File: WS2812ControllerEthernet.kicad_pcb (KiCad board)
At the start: 2 copper layers, 26.9 x 59.8 mm, 11 parts, among them J1 Conn_01x04_Male, J2 Conn_01x03_Male, J3 Conn_01x04_Male, J4 Conn_01x02_Male, U1 WT32_ETH01

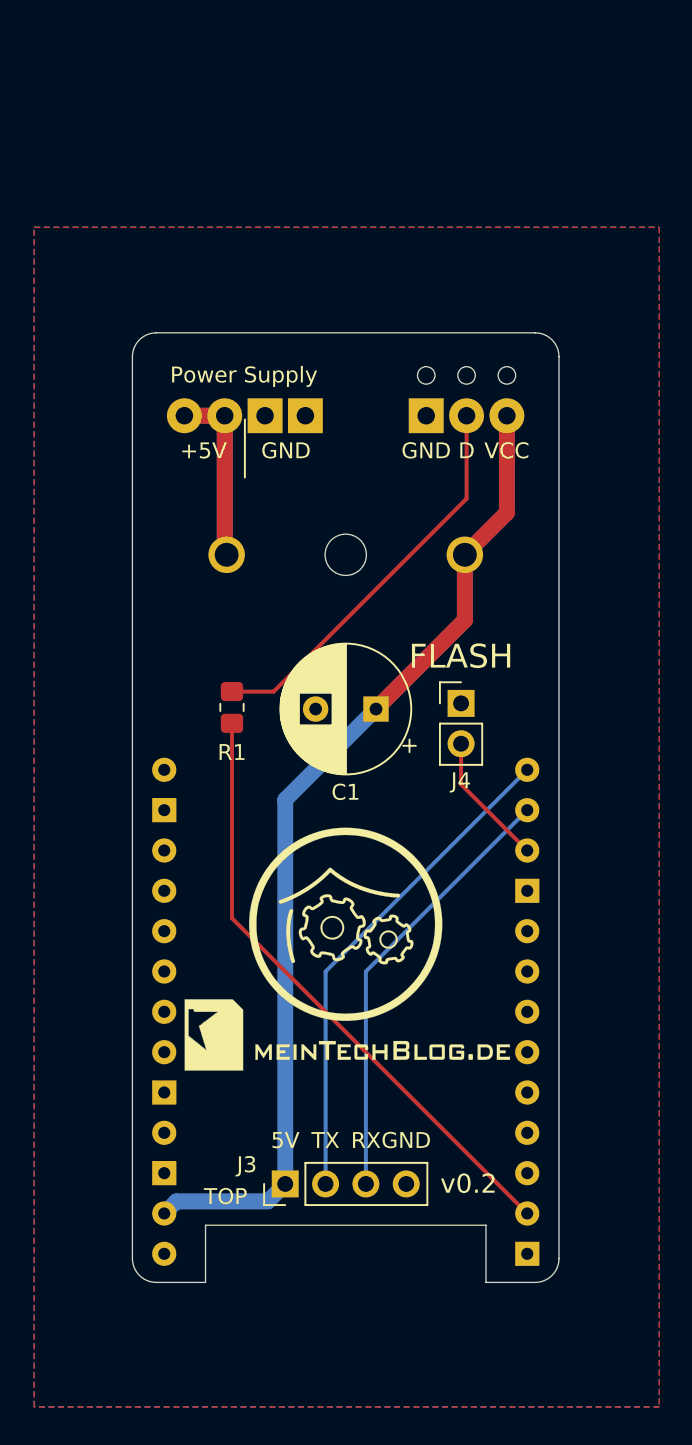
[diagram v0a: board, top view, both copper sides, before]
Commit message: Added level shifter
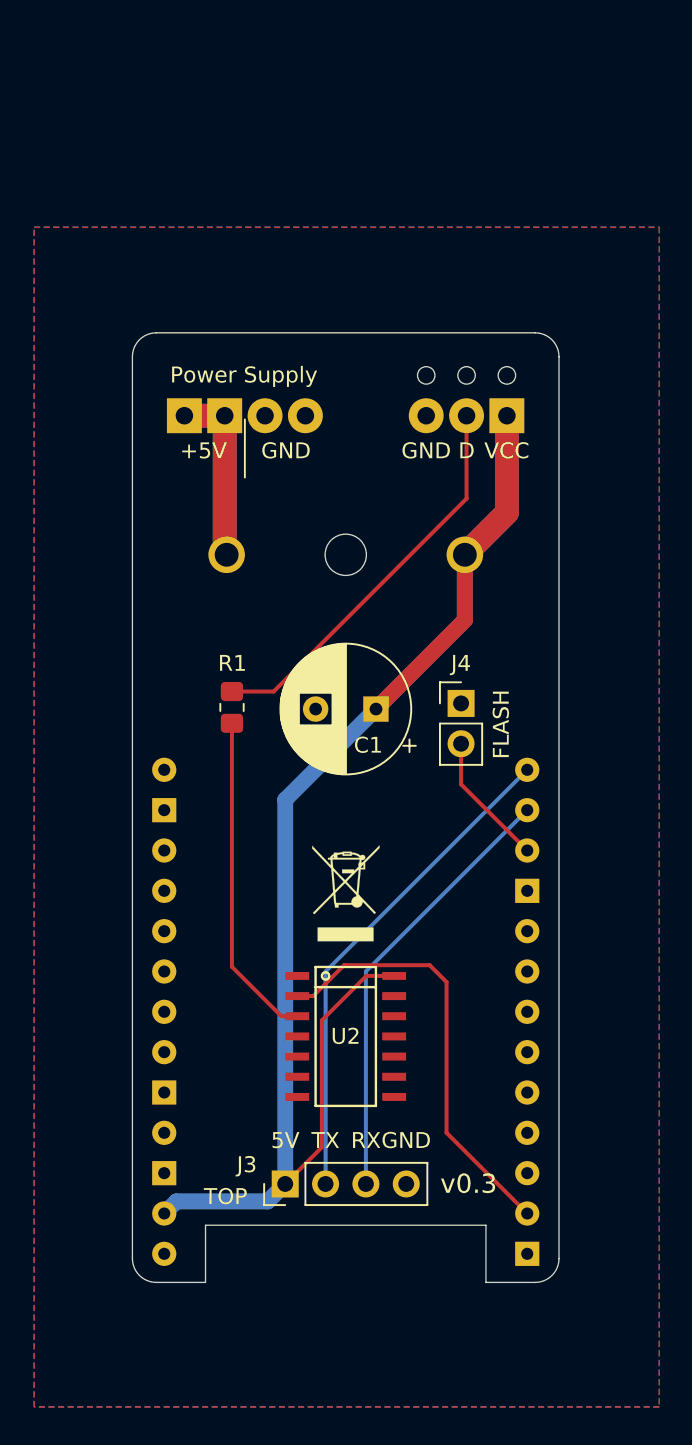
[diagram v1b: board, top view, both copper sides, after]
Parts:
- added U2: SN74AHCT125, halibs:SN74AHCT125D, F.Cu at (146.6, 90.5)
- G*** (x2): moved to B.Cu
- REF**: moved to F.Cu
- moved REF** 18.4 mm to (146.6, 87.3), turned to 0 degrees
- moved G*** 8.41 mm to (139.1, 92.5), turned to 90 degrees
- moved G*** 5.88 mm to (148.4, 94.8), turned to 90 degrees
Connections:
- net /DATA renamed Net-(J2-Pad2)
- R1 pad 2: GPIO2 -> DATA
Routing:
- net DATA: track 0.00 -> 20.7 mm
- net +5V: track 84.6 -> 101.6 mm
- net GPIO2: track 38.6 -> 27.3 mm
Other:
- net class Fet: trace_width 1 -> 1.5
- board text added: "5A max."
- board text added: "v0.3"
- board text removed: "Max. 6A !"
- board text removed: "v0.2"

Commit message: Updated to KiCad 6
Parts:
- U1: footprint halibs:WT32_ETH01 -> haus-automatisierung:WT32_ETH01
- U2: footprint halibs:SN74AHCT125D -> haus-automatisierung:SN74AHCT125D
- moved G*** 1.93 mm to (146.6, 94.2)
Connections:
- U1 pad 1: Net-(U1-Pad1) -> unconnected-(U1-Pad1)
- U1 pad 10: Net-(U1-Pad10) -> unconnected-(U1-Pad10)
- U1 pad 13: Net-(U1-Pad13) -> unconnected-(U1-Pad13)
- U1 pad 17: Net-(U1-Pad17) -> unconnected-(U1-Pad17)
- U1 pad 18: Net-(U1-Pad18) -> unconnected-(U1-Pad18)
- U1 pad 19: Net-(U1-Pad19) -> unconnected-(U1-Pad19)
- U1 pad 2: Net-(U1-Pad2) -> unconnected-(U1-Pad2)
- U1 pad 20: Net-(U1-Pad20) -> unconnected-(U1-Pad20)
- U1 pad 21: Net-(U1-Pad21) -> unconnected-(U1-Pad21)
- U1 pad 22: Net-(U1-Pad22) -> unconnected-(U1-Pad22)
- U1 pad 23: Net-(U1-Pad23) -> unconnected-(U1-Pad23)
- U1 pad 24: Net-(U1-Pad24) -> unconnected-(U1-Pad24)
- U1 pad 26: Net-(U1-Pad26) -> unconnected-(U1-Pad26)
- U1 pad 3: Net-(U1-Pad3) -> unconnected-(U1-Pad3)
- U1 pad 4: Net-(U1-Pad4) -> unconnected-(U1-Pad4)
- U1 pad 5: Net-(U1-Pad5) -> unconnected-(U1-Pad5)
- U1 pad 6: Net-(U1-Pad6) -> unconnected-(U1-Pad6)
- U1 pad 7: Net-(U1-Pad7) -> unconnected-(U1-Pad7)
- U1 pad 8: Net-(U1-Pad8) -> unconnected-(U1-Pad8)
- U1 pad 9: Net-(U1-Pad9) -> unconnected-(U1-Pad9)
- U2 pad 11: Net-(U2-Pad11) -> unconnected-(U2-Pad11)
- U2 pad 12: Net-(U2-Pad12) -> unconnected-(U2-Pad12)
- U2 pad 5: Net-(U2-Pad5) -> unconnected-(U2-Pad5)
- U2 pad 6: Net-(U2-Pad6) -> unconnected-(U2-Pad6)
- U2 pad 8: Net-(U2-Pad8) -> unconnected-(U2-Pad8)
- U2 pad 9: Net-(U2-Pad9) -> unconnected-(U2-Pad9)
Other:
- net class Default removed
- net class Fet removed

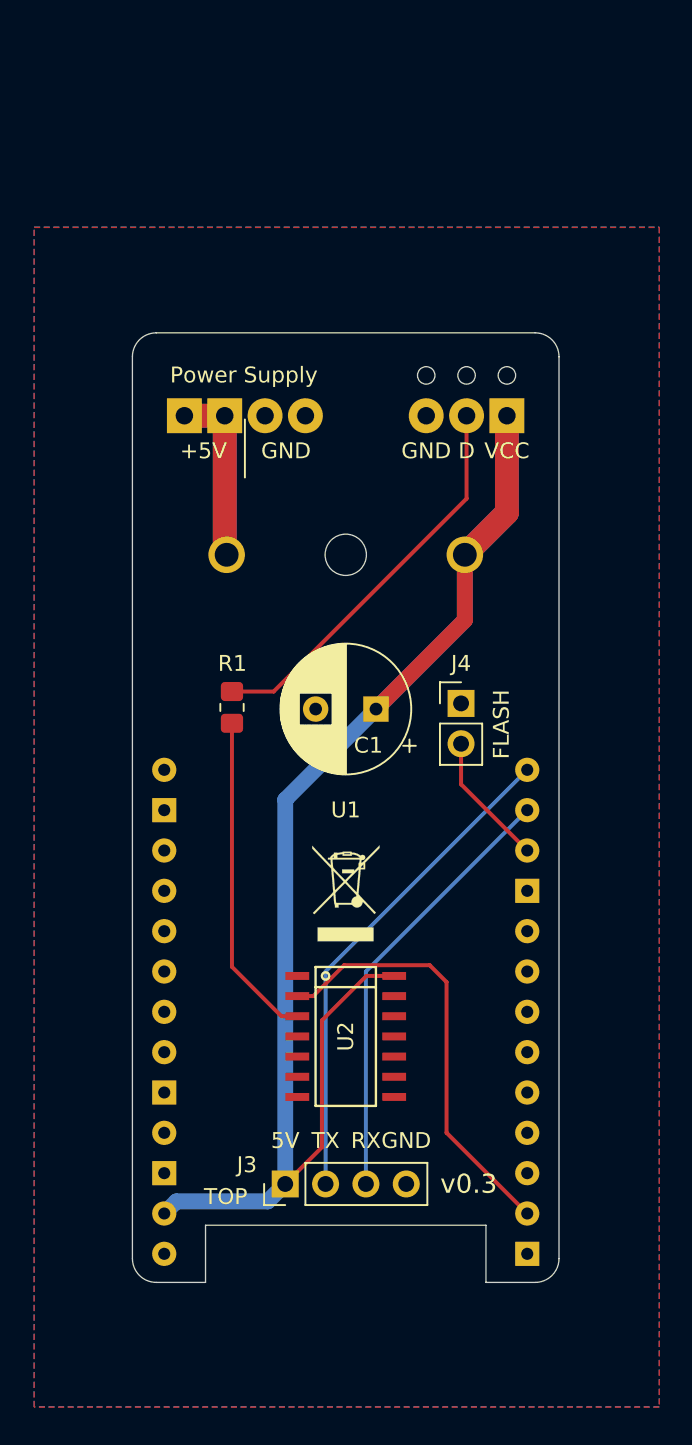
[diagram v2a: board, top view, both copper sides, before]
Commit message: Updated layout
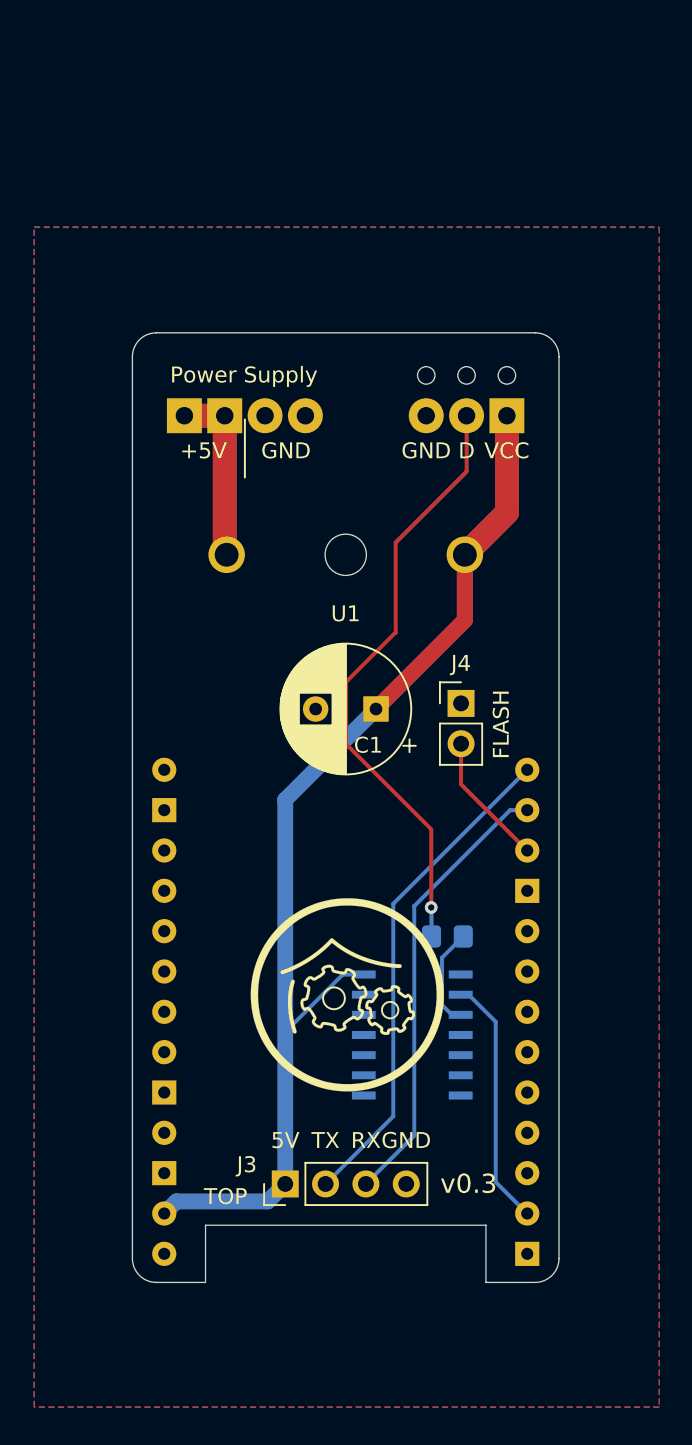
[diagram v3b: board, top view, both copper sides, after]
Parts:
- removed the G*** at (139.1, 92.5)
- added G***: LOGO, haus-automatisierung:QRCode-hausauto_10mm, B.Cu at (144.0, 85.8)
- added G***: LOGO, haus-automatisierung:meintechblog, B.Cu at (139.2, 91.8)
- G***: moved to F.Cu
- R1, REF**, U2: moved to B.Cu
- moved R1 19.8 mm to (153.0, 90.0), turned to 0 degrees
- moved REF** 14.2 mm to (139.0, 75.2), turned to 180 degrees
- moved U2 4.19 mm to (150.7, 90.4), turned to 180 degrees
- moved G*** 0.55 mm to (146.7, 93.7), turned to 0 degrees
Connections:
- U1 pad 17: unconnected-(U1-Pad17) -> GND
- U1 pad 2: unconnected-(U1-Pad2) -> GND
- U1 pad 26: unconnected-(U1-Pad26) -> GND
- U1 pad 9: unconnected-(U1-Pad9) -> GND
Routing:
- net DATA: track 20.7 -> 6.30 mm
- net Net-(J2-Pin_2): track 25.0 -> 38.2 mm, vias 0 -> 1
- net GPIO2: track 27.3 -> 15.8 mm
- net +5V: track 101.4 -> 90.9 mm
- net /RX: track 27.7 -> 28.4 mm

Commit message: Added additional GPIO for strip
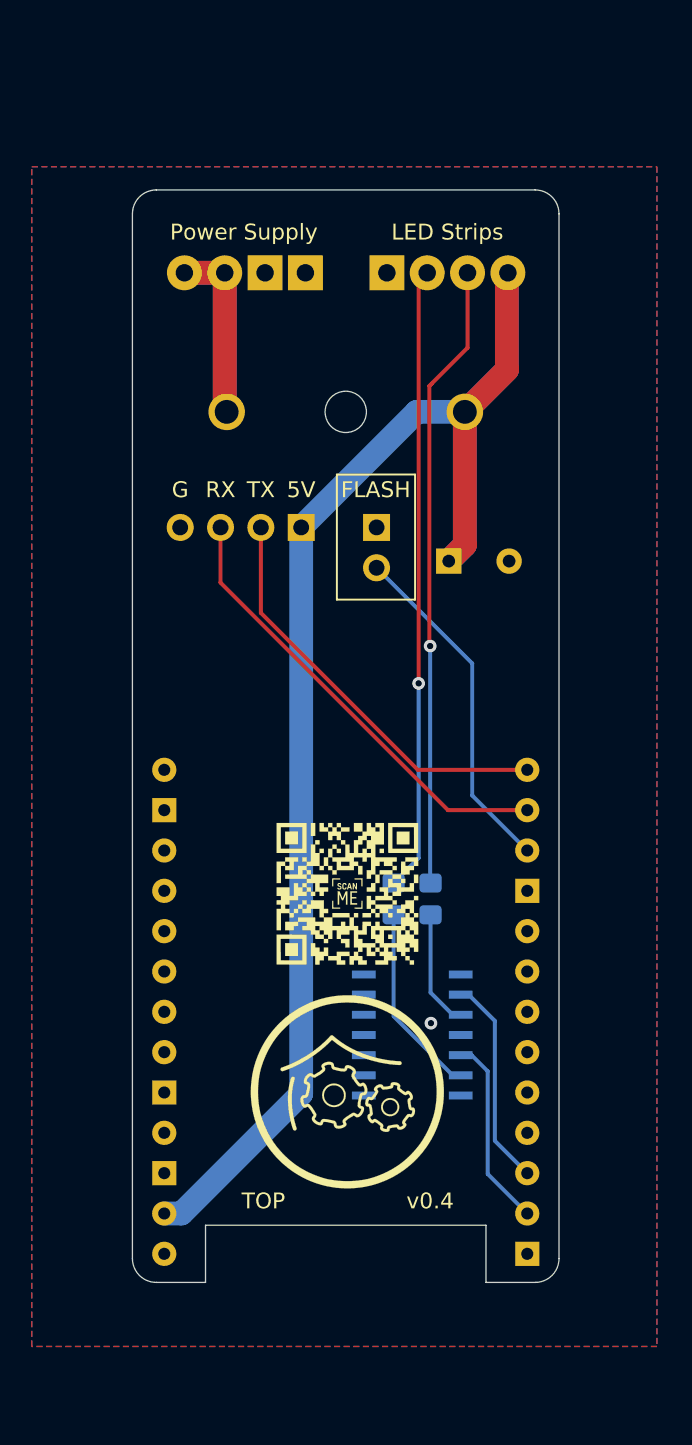
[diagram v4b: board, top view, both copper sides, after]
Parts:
- removed the G*** at (146.7, 93.7)
- removed the G*** at (139.2, 91.8)
- removed REF**: WEEE-Logo_4.2x6mm_SilkScreen, Symbol:WEEE-Logo_4.2x6mm_SilkScreen
- added G***: LOGO, haus-automatisierung:Logo, F.Cu at (146.7, 99.8)
- added R2: R, Resistor_SMD:R_0805_2012Metric_Pad1.20x1.40mm_HandSolder, B.Cu at (149.6, 87.7)
- C1, J3, J4: moved to B.Cu
- F1: footprint halibs:Fuse-PTF75_Stelvio -> haus-automatisierung:Fuse-PTF75_Stelvio
- G2: renamed from G***; moved to F.Cu
- J2: value Conn_01x03_Male -> Conn_01x04_Male; footprint TerminalBlock_Phoenix:TerminalBlock_Phoenix_MPT-0,5-3-2.54_1x03_P2.54mm_Horizontal -> TerminalBlock_Phoenix:TerminalBlock_Phoenix_MPT-0,5-4-2.54_1x04_P2.54mm_Horizontal
- moved J3 41.4 mm to (143.8, 64.3)
- moved J4 12.3 mm to (148.5, 64.3), turned to 180 degrees
- moved C1 10.4 mm to (153.0, 66.4), turned to 0 degrees
- moved J2 9.34 mm to (149.2, 48.2)
- moved F1 9.00 mm to (146.6, 52.3)
- moved J1 9.00 mm to (136.4, 48.2)
- moved G2 3.07 mm to (146.7, 87.3), turned to 0 degrees
- moved R1 2.59 mm to (151.9, 87.7), turned to -90 degrees
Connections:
- net DATA renamed DATA1
- J2 pad 3: +5V -> Net-(J2-Pin_3)
- R1 pad 1: Net-(J2-Pin_2) -> Net-(J2-Pin_3)
- U1 pad 24: unconnected-(U1-IO4-Pad24) -> GPIO4
- U2 pad 2: GPIO2 -> GPIO4
- U2 pad 5: unconnected-(U2-2A-Pad5) -> GPIO2
- U2 pad 6: unconnected-(U2-2Y-Pad6) -> DATA2
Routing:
- net Net-(J2-Pin_3): track 0.00 -> 39.5 mm, vias 0 -> 1
- net IO0: track 8.45 -> 21.7 mm
- net GPIO4: track 0.00 -> 13.3 mm
- net DATA2: track 0.00 -> 12.2 mm
- net +5V: track 90.9 -> 100.1 mm
- net /TX: track 31.3 -> 26.3 mm
- net GPIO2: track 15.8 -> 12.1 mm
- net DATA1: track 6.30 -> 7.94 mm
- net Net-(J2-Pin_2): track 38.2 -> 39.3 mm
- net GND: vias 0 -> 1
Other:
- board size 26.9 x 59.8 mm -> 26.9 x 68.8 mm
- board text added: "+"
- board text added: "D2"
- board text added: "D4"
- board text added: "G"
- board text added: "LED Strips"
- board text added: "v0.4"
- board text removed: "D"
- board text removed: "VCC"
- board text removed: "v0.3"

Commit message: KiCad 8
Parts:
- removed the G*** at (146.7, 99.8)
- added G***: LOGO, haus-automatisierung:Logo2024, F.Cu at (146.7, 99.2)
- added J3: Conn_01x03_Pin, TerminalBlock_Phoenix:TerminalBlock_Phoenix_MPT-0,5-3-2.54_1x03_P2.54mm_Horizontal, B.Cu at (138.1, 47.0)
- J1: value Conn_01x04_Male -> Barrel_Jack_MountingPin; footprint TerminalBlock_Phoenix:TerminalBlock_Phoenix_MPT-0,5-4-2.54_1x04_P2.54mm_Horizontal -> Connector_BarrelJack:BarrelJack_Wuerth_6941xx301002
- J2: value Conn_01x04_Male -> Conn_01x03_Pin; footprint TerminalBlock_Phoenix:TerminalBlock_Phoenix_MPT-0,5-4-2.54_1x04_P2.54mm_Horizontal -> TerminalBlock_Phoenix:TerminalBlock_Phoenix_MPT-0,5-3-2.54_1x03_P2.54mm_Horizontal
- moved J1 18.8 mm to (145.1, 64.8), turned to -90 degrees
- moved J4 13.3 mm to (139.9, 77.0), turned to 180 degrees
- moved C1 12.6 mm to (140.5, 65.3), turned to 180 degrees
- moved J5 10.9 mm to (153.0, 74.1), turned to -90 degrees
- moved F1 7.60 mm to (146.6, 59.9), turned to 0 degrees
- moved J2 1.46 mm to (149.9, 47.0)
- renumbered J3 to J4, J4 to J5
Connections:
- J1 pad 2: /SUPPLY -> GND
- J1 pad 3: GND -> (no net)
- J2 pad 2: Net-(J2-Pin_2) -> /D4
- J2 pad 3: Net-(J2-Pin_3) -> +5V
- R1 pad 1: Net-(J2-Pin_3) -> /D4
- R2 pad 1: Net-(J2-Pin_2) -> /D2
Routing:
- net /D4: track 0.00 -> 50.6 mm
- net /D2: track 0.00 -> 45.3 mm
- net Net-(J2-Pin_3): track 39.5 -> 0.00 mm, vias 1 -> 0
- net Net-(J2-Pin_2): track 39.3 -> 0.00 mm, vias 1 -> 0
- net /RX: track 28.7 -> 18.1 mm
- net IO0: track 21.7 -> 11.5 mm
- net /TX: track 26.3 -> 18.1 mm
- net +5V: track 100.1 -> 107.1 mm
- net /SUPPLY: track 22.7 -> 26.8 mm
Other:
- board size 26.9 x 68.8 mm -> 26.9 x 70.6 mm
- board text added: "v1.0"
- board text removed: "+5V"
- board text removed: "GND"
- board text removed: "LED Strips"
- board text removed: "Power Supply"
- board text removed: "v0.4"

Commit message: v1.0
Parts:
- removed G2: LOGO, haus-automatisierung:QRCode-hausauto_10mm
- moved G*** 2.54 mm to (146.7, 96.6)
- moved J4 1.72 mm to (141.6, 77.0)
- moved J2 0.50 mm to (149.9, 46.5)
- moved J3 0.50 mm to (138.1, 46.5)
- moved F1 0.30 mm to (146.6, 59.6)
- moved J1 0.10 mm to (145.1, 64.8)
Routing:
- net +5V: track 107.1 -> 80.9 mm
- net /D4: track 50.6 -> 48.0 mm
- net /SUPPLY: track 26.8 -> 28.6 mm
- net /TX: track 18.1 -> 16.4 mm
- net /RX: track 18.1 -> 16.4 mm
- net /D2: track 45.3 -> 43.9 mm

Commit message: v1.1
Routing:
- net +5V: track 80.9 -> 103.2 mm
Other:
- board text added: "v1.1"
- board text removed: "v1.0"
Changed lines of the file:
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@@
 	(title_block
 		(title "WS2812-Controller Ethernet")
-		(date "2024-05-17")
-		(rev "1.0")
+		(date "2024-05-24")
+		(rev "1.1")
 		(company "haus-automatisierung.com")
 		(comment 1 "Matthias Kleine")
@@
 		(tags "CP Radial series Radial pin pitch 3.80mm  diameter 8mm Electrolytic Capacitor")
 		(property "Reference" "C1"
-			(at 0.484601 2.286 90)
+			(at 5.75 4.125 90)
 			(layer "B.SilkS")
 			(effects
@@
 		(at 146.560001 59.5775)
 		(property "Reference" "F1"
-			(at 0 -1.5 90)
+			(at 0 -8.0025 90)
 			(layer "B.SilkS")
 			(effects
@@
 		(tags "THT Terminal Block Phoenix MPT-0,5-3-2.54 pitch 2.54mm size 8.08x6.2mm^2 drill 1.1mm pad 2.2mm")
 		(property "Reference" "J2"
-			(at 2.54 2.16 0)
+			(at 7.614999 0 90)
 			(layer "B.SilkS")
 			(effects
@@
 		(tags "THT Terminal Block Phoenix MPT-0,5-3-2.54 pitch 2.54mm size 8.08x6.2mm^2 drill 1.1mm pad 2.2mm")
 		(property "Reference" "J3"
-			(at 2.54 2.16 0)
+			(at 7.649459 0 90)
 			(layer "B.SilkS")
 			(effects
@@
 		)
 	)
-	(gr_text "v1.0"
+	(gr_text "v1.1"
 		(at 151.875 106.675 0)
 		(layer "F.SilkS")
@@
 		)
 	)
+	(gr_text "G"
+		(at 138.125541 42.4 -180)
+		(layer "F.SilkS")
+		(effects
+			(font
+				(size 1 1)
+				(thickness 0.15)
+			)
+		)
+	)
+	(gr_text "+"
+		(at 154.990001 42.4 -180)
+		(layer "F.SilkS")
+		(effects
+			(font
+				(size 1 1)
+				(thickness 0.15)
+			)
+		)
+	)
 	(gr_text "TX"
 		(at 139.225 79.520001 90)
@@
 		)
 	)
+	(gr_text "D2"
+		(at 140.665541 42.4 -180)
+		(layer "F.SilkS")
+		(effects
+			(font
+				(size 1 1)
+				(thickness 0.15)
+			)
+		)
+	)
+	(gr_text "G"
+		(at 149.910001 42.4 -180)
+		(layer "F.SilkS")
+		(effects
+			(font
+				(size 1 1)
+				(thickness 0.15)
+			)
+		)
+	)
 	(gr_text "G"
 		(at 139.225 84.600001 90)
@@
 		)
 	)
+	(gr_text "+"
+		(at 143.205541 42.4 -180)
+		(layer "F.SilkS")
+		(effects
+			(font
+				(size 1 1)
+				(thickness 0.15)
+			)
+		)
+	)
+	(gr_text "D4"
+		(at 152.450001 42.4 -180)
+		(layer "F.SilkS")
+		(effects
+			(font
+				(size 1 1)
+				(thickness 0.15)
+			)
+		)
+	)
+	(dimension
+		(type aligned)
+		(layer "F.SilkS")
+		(pts
+			(xy 163.485541 41.2) (xy 163.490001 111.8)
+		)
+		(height -4.515347)
+		(gr_text "70.6000 mm"
+			(at 169.153118 76.499642 270.0036195)
+			(layer "F.SilkS")
+			(effects
+				(font
+					(size 1 1)
+					(thickness 0.15)
+				)
+			)
+		)
+		(format
+			(prefix "")
+			(suffix "")
+			(units 3)
+			(units_format 1)
+			(precision 4)
+		)
+		(style
+			(thickness 0.12)
+			(arrow_length 1.27)
+			(text_position_mode 0)
+			(extension_height 0.58642)
+			(extension_offset 0.5) keep_text_aligned)
+	)
 	(dimension
 		(type aligned)
@@
 	)
 	(segment
+		(start 140.525 65.3)
+		(end 140.525 75.910001)
+		(width 1.5)
+		(layer "B.Cu")
+		(net 1)
+	)
+	(segment
+		(start 138.95 79.477995)
+		(end 138.95 88.875)
+		(width 1.5)
+		(layer "B.Cu")
+		(net 1)
+	)
+	(segment
+		(start 147.699 92.4089)
+		(end 142.4839 92.4089)
+		(width 0.25)
+		(layer "B.Cu")
+		(net 1)
+	)
+	(segment
+		(start 138.95 88.875)
+		(end 138.95 104.724002)
+		(width 1.5)
+		(layer "B.Cu")
+		(net 1)
+	)
+	(segment
 		(start 138.95 104.724002)
 		(end 136.214001 107.460001)
@@
 	)
 	(segment
+		(start 142.4839 92.4089)
+		(end 138.95 88.875)
+		(width 0.25)
+		(layer "B.Cu")
+		(net 1)
+	)
+	(segment
 		(start 141.595 76.980001)
 		(end 141.447994 76.980001)
@@
 	)
 	(segment
-		(start 138.95 79.477995)
-		(end 138.95 104.724002)
+		(start 140.525 75.910001)
+		(end 141.595 76.980001)
 		(width 1.5)
 		(layer "B.Cu")

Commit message: v2.0
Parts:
- U1: footprint haus-automatisierung:WT32_ETH01 -> haus-automatisierung:WT32_ETH01_long
- moved J2 3.30 mm to (149.9, 43.2)
- moved J3 3.30 mm to (138.1, 43.2)
- moved C1 3.30 mm to (140.5, 62.0)
- moved F1 3.30 mm to (146.6, 56.3)
- moved J1 3.30 mm to (145.1, 61.5)
- moved J5 3.00 mm to (150.0, 74.1)
- moved R1 2.00 mm to (149.9, 87.7)
- moved R2 2.00 mm to (147.6, 87.7)
- moved U2 2.00 mm to (148.7, 90.4)
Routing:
- net +5V: track 103.2 -> 113.4 mm
- net /D4: track 48.0 -> 50.5 mm
- net /D2: track 43.9 -> 46.3 mm
- net /SUPPLY: track 28.6 -> 26.1 mm
- net GPIO4: track 13.3 -> 15.3 mm
- net GPIO2: track 12.1 -> 14.1 mm
- net IO0: track 11.5 -> 12.7 mm
- net DATA1: track 7.94 -> 6.88 mm
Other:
- board size 26.9 x 70.6 mm -> 26.9 x 73.9 mm
- board text added: "v2.0"
- board text removed: "v1.1"
